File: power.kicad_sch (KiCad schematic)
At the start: 50 parts, among them U5 TPS82084SIL, U6 TPS82084SIL, U7 TPS7A8801RTJR, U901 TPS7A8801RTJR

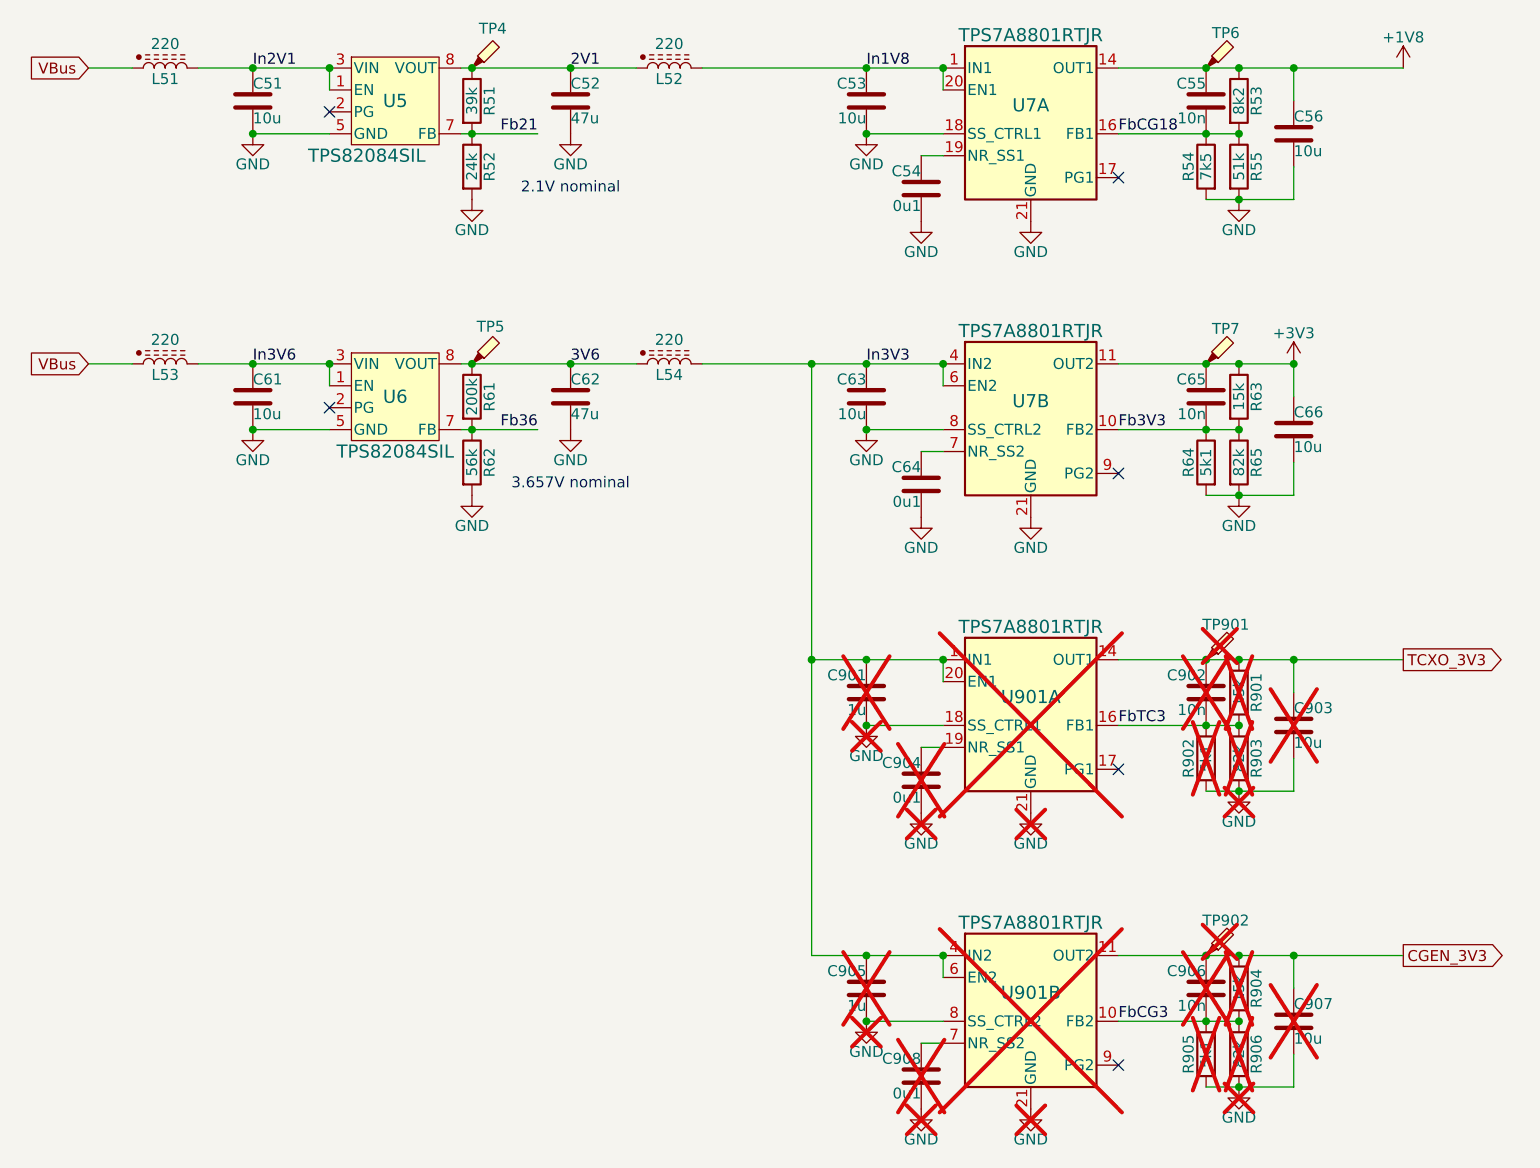
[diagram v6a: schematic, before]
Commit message: Route extint.
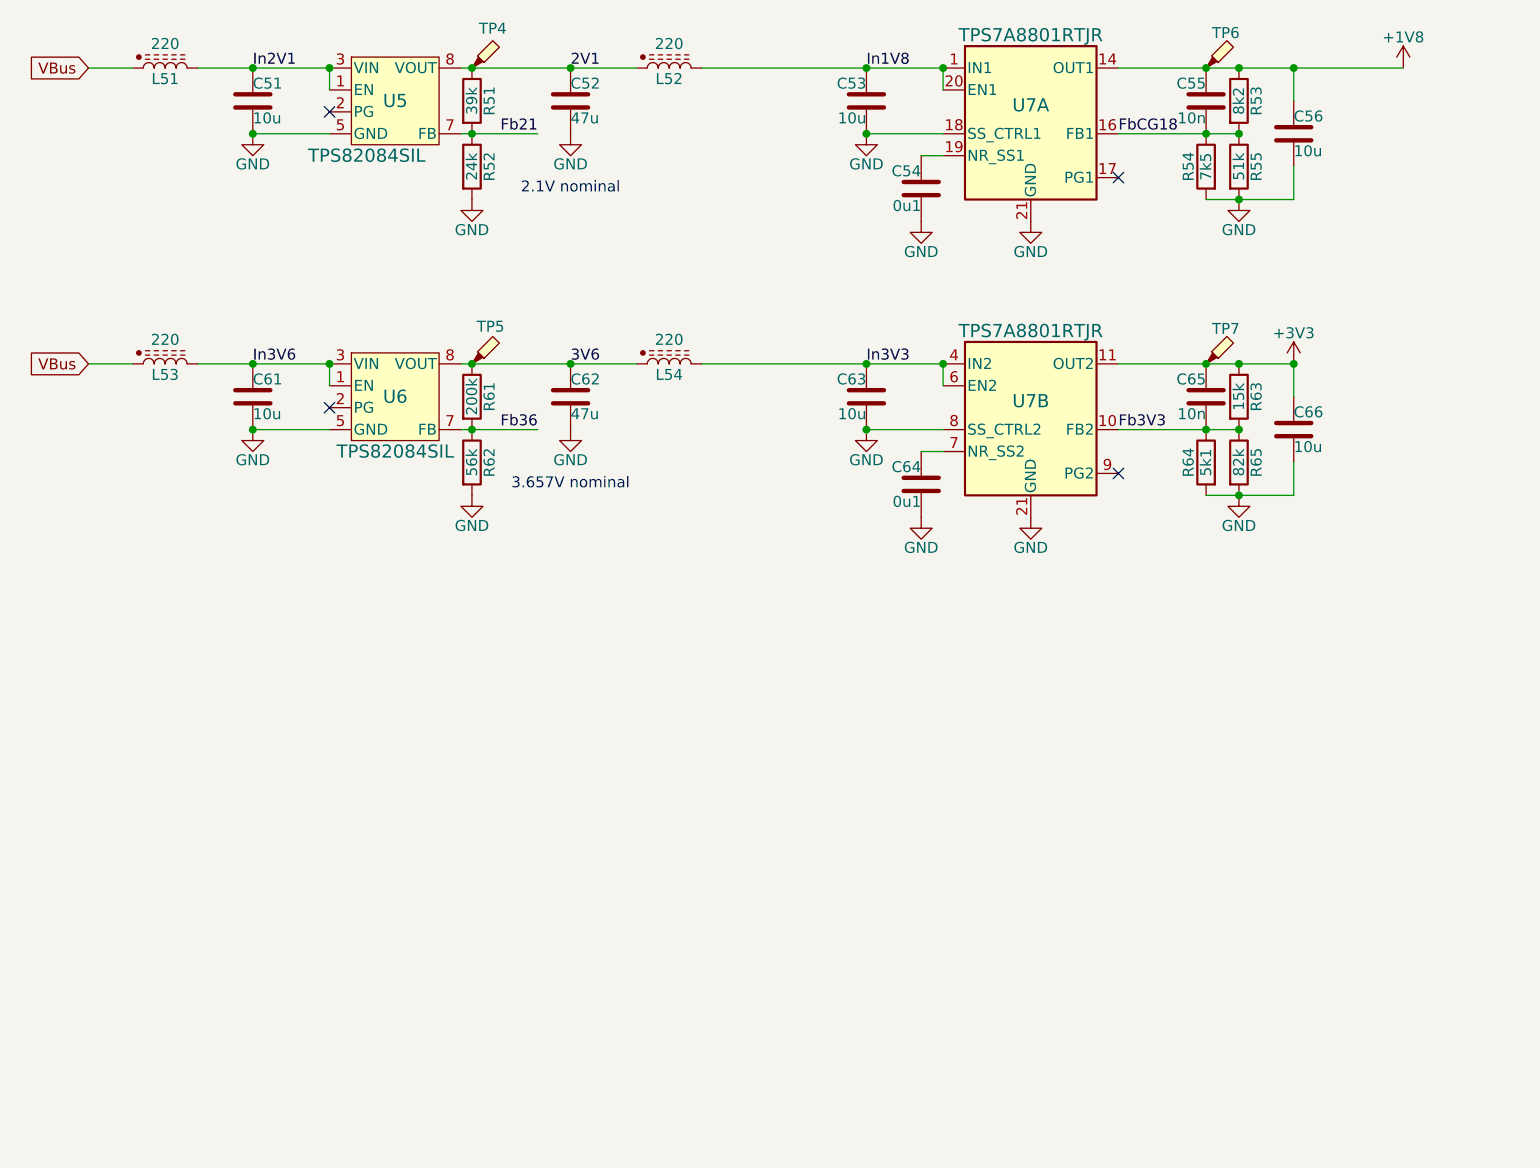
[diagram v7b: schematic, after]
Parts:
- removed C901, C905: 1u, Capacitor_SMD:C_0402_1005Metric, symbol Device:C
- removed C902, C906: 10n, Capacitor_SMD:C_0402_1005Metric, symbol Device:C
- removed C903, C907: 10u, Capacitor_SMD:C_0402_1005Metric, symbol Device:C
- removed C904, C908: 0u1, Capacitor_SMD:C_0402_1005Metric, symbol Device:C
- removed R901, R904: 15k, Resistor_SMD:R_0402_1005Metric, symbol Device:R
- removed R902, R905: 5k1, Resistor_SMD:R_0402_1005Metric, symbol Device:R
- removed R903, R906: 82k, Resistor_SMD:R_0603_1608Metric, symbol Device:R
- removed TP901, TP902: TestPoint_Probe, Parts:TestPoint, symbol Connector:TestPoint_Probe
- removed U901: TPS7A8801RTJR, Parts:QFN-20-1EP_4x4mm_P0.5mm_EP2.7x2.7mm, symbol Parts:TPS7A8801RTJR
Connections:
- no-connect marks 6 -> 4
